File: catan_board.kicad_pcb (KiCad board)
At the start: 2 copper layers, 90 x 78.1 mm, 42 parts

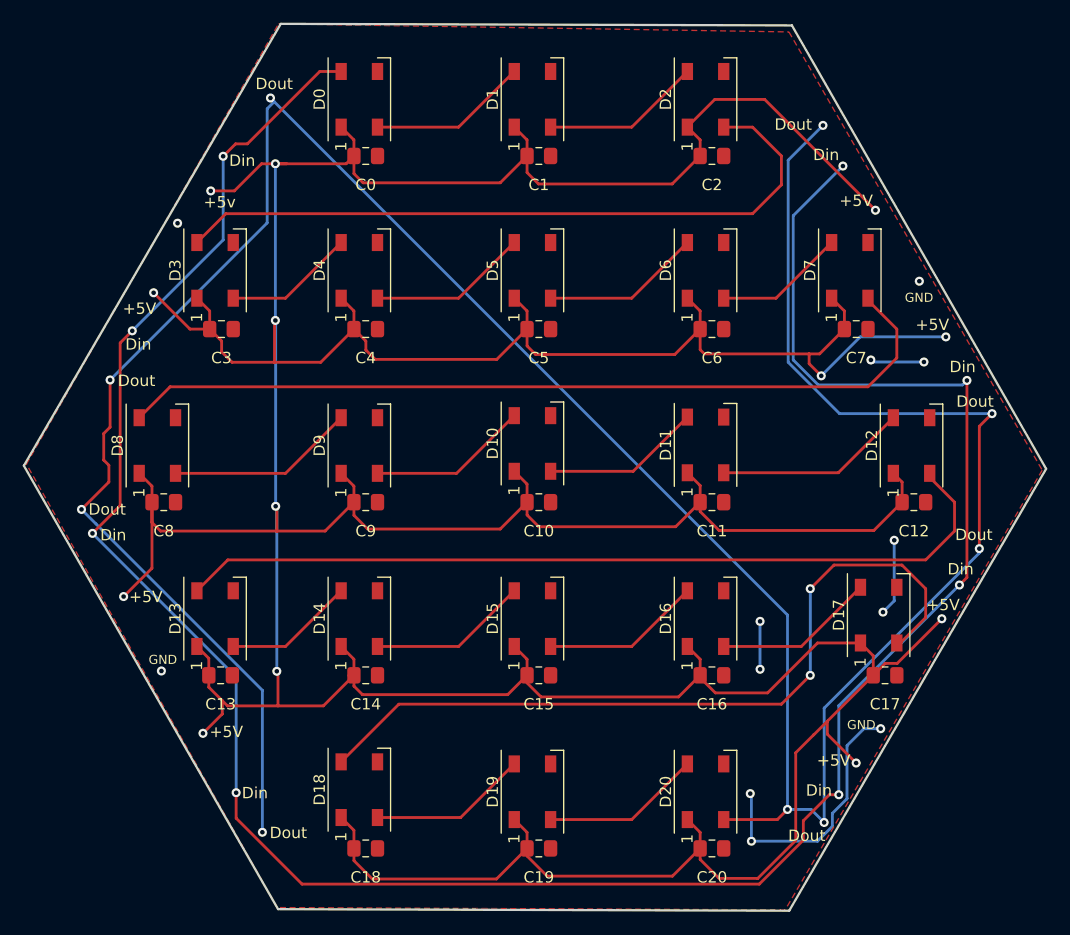
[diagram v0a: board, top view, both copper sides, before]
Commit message: 5v rail added to back copper
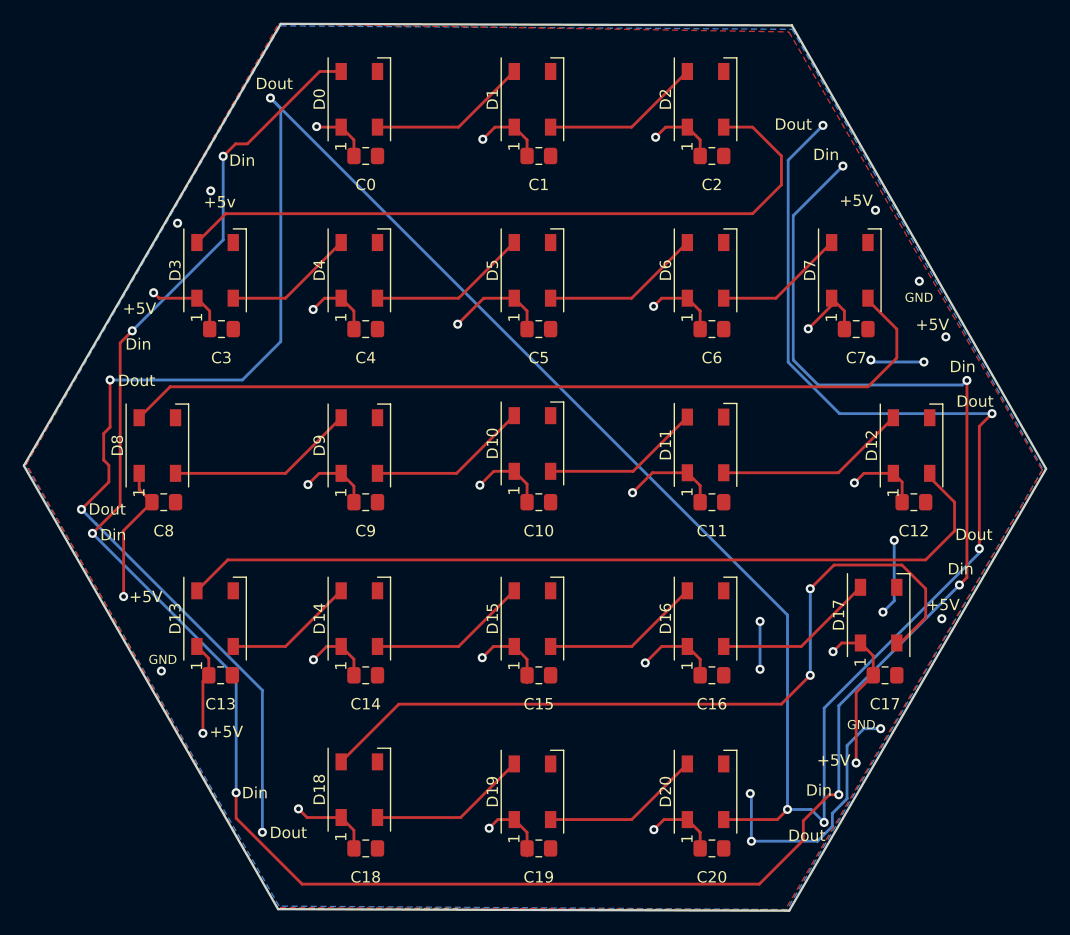
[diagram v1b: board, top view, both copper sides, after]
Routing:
- net +5V: track 514.0 -> 157.5 mm, vias 13 -> 26
- net Net-(D20-Pad2): track 253.5 -> 261.3 mm
- added copper zone on B.Cu, net +5V

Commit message: pcb is done
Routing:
- net Net-(D20-Pad2): track 261.3 -> 157.5 mm, vias 9 -> 7
- net GND: track 38.8 -> 6.73 mm, vias 12 -> 6
- net Net-(D0-Pad4): track 217.9 -> 198.5 mm, vias 8 -> 7
- net +5V: track 157.5 -> 151.2 mm, vias 26 -> 23

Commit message: its been a while
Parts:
- added ?: PinHeader_1x01_P1.00mm_Vertical, Connector_PinHeader_1.00mm:PinHeader_1x01_P1.00mm_Vertical, F.Cu at (163.6, 64.0)
- added ?: PinHeader_1x01_P1.00mm_Vertical, Connector_PinHeader_1.00mm:PinHeader_1x01_P1.00mm_Vertical, F.Cu at (104.0, 107.6)
- added ?: PinHeader_1x01_P1.00mm_Vertical, Connector_PinHeader_1.00mm:PinHeader_1x01_P1.00mm_Vertical, F.Cu at (101.9, 102.6)
- added ?: PinHeader_1x01_P1.00mm_Vertical, Connector_PinHeader_1.00mm:PinHeader_1x01_P1.00mm_Vertical, F.Cu at (101.4, 83.4)
- added ?: PinHeader_1x01_P1.00mm_Vertical, Connector_PinHeader_1.00mm:PinHeader_1x01_P1.00mm_Vertical, F.Cu at (104.6, 77.8)
- added ?: PinHeader_1x01_P1.00mm_Vertical, Connector_PinHeader_1.00mm:PinHeader_1x01_P1.00mm_Vertical, F.Cu at (109.3, 70.6)
- added ?: PinHeader_1x01_P1.00mm_Vertical, Connector_PinHeader_1.00mm:PinHeader_1x01_P1.00mm_Vertical, F.Cu at (113.1, 64.7)
- added ?: PinHeader_1x01_P1.00mm_Vertical, Connector_PinHeader_1.00mm:PinHeader_1x01_P1.00mm_Vertical, F.Cu at (166.3, 69.6)
- added ?: PinHeader_1x01_P1.00mm_Vertical, Connector_PinHeader_1.00mm:PinHeader_1x01_P1.00mm_Vertical, F.Cu at (173.4, 81.0)
- added ?: PinHeader_1x01_P1.00mm_Vertical, Connector_PinHeader_1.00mm:PinHeader_1x01_P1.00mm_Vertical, F.Cu at (175.7, 85.0)
- added ?: PinHeader_1x01_P1.00mm_Vertical, Connector_PinHeader_1.00mm:PinHeader_1x01_P1.00mm_Vertical, F.Cu at (177.7, 99.2)
- added ?: PinHeader_1x01_P1.00mm_Vertical, Connector_PinHeader_1.00mm:PinHeader_1x01_P1.00mm_Vertical, F.Cu at (175.1, 103.6)
- added ?: PinHeader_1x01_P1.00mm_Vertical, Connector_PinHeader_1.00mm:PinHeader_1x01_P1.00mm_Vertical, F.Cu at (165.5, 118.7)
- added ?: PinHeader_1x01_P1.00mm_Vertical, Connector_PinHeader_1.00mm:PinHeader_1x01_P1.00mm_Vertical, F.Cu at (162.7, 124.4)
- added ?: PinHeader_1x01_P1.00mm_Vertical, Connector_PinHeader_1.00mm:PinHeader_1x01_P1.00mm_Vertical, F.Cu at (114.5, 124.0)
- added ?: PinHeader_1x01_P1.00mm_Vertical, Connector_PinHeader_1.00mm:PinHeader_1x01_P1.00mm_Vertical, F.Cu at (111.0, 117.3)
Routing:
- net GND: track 6.73 -> 9.21 mm, vias 6 -> 3
- net Net-(D20-Pad2): track 157.5 -> 156.5 mm, vias 7 -> 3
- net +5V: track 151.2 -> 151.3 mm, vias 23 -> 19
- net Net-(D0-Pad4): vias 7 -> 3

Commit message: change ports to header pins
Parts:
- removed ? (x16): PinHeader_1x01_P1.00mm_Vertical, Connector_PinHeader_1.00mm:PinHeader_1x01_P1.00mm_Vertical
- added GND: PinHeader_1x04_P2.54mm_Vertical, Connector_PinHeader_2.54mm:PinHeader_1x04_P2.54mm_Vertical, F.Cu at (114.3, 62.7)
- added GND: PinHeader_1x04_P2.54mm_Vertical, Connector_PinHeader_2.54mm:PinHeader_1x04_P2.54mm_Vertical, F.Cu at (110.5, 118.1)
- added GND: PinHeader_1x04_P2.54mm_Vertical, Connector_PinHeader_2.54mm:PinHeader_1x04_P2.54mm_Vertical, F.Cu at (161.9, 62.3)
- added GND: PinHeader_1x04_P2.54mm_Vertical, Connector_PinHeader_2.54mm:PinHeader_1x04_P2.54mm_Vertical, F.Cu at (165.1, 117.5)
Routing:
- net Net-(D20-Pad2): track 156.5 -> 179.0 mm, vias 3 -> 2
- net Net-(D0-Pad4): track 198.5 -> 185.2 mm, vias 3 -> 1
- net +5V: track 151.3 -> 163.2 mm, vias 19 -> 20
- net GND: track 9.21 -> 0.00 mm, vias 3 -> 0
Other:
- net class Default removed
- board text removed: "GND"
